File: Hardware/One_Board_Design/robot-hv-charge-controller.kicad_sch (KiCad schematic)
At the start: 14 parts, among them J2 UART_CONN, J3 XT30PW-M, J4 Conn_01x02, J5 XT60PW-M, J6 Conn_01x02, J7 XT60PW-M, J8 Conn_01x03, J9 Conn_01x02

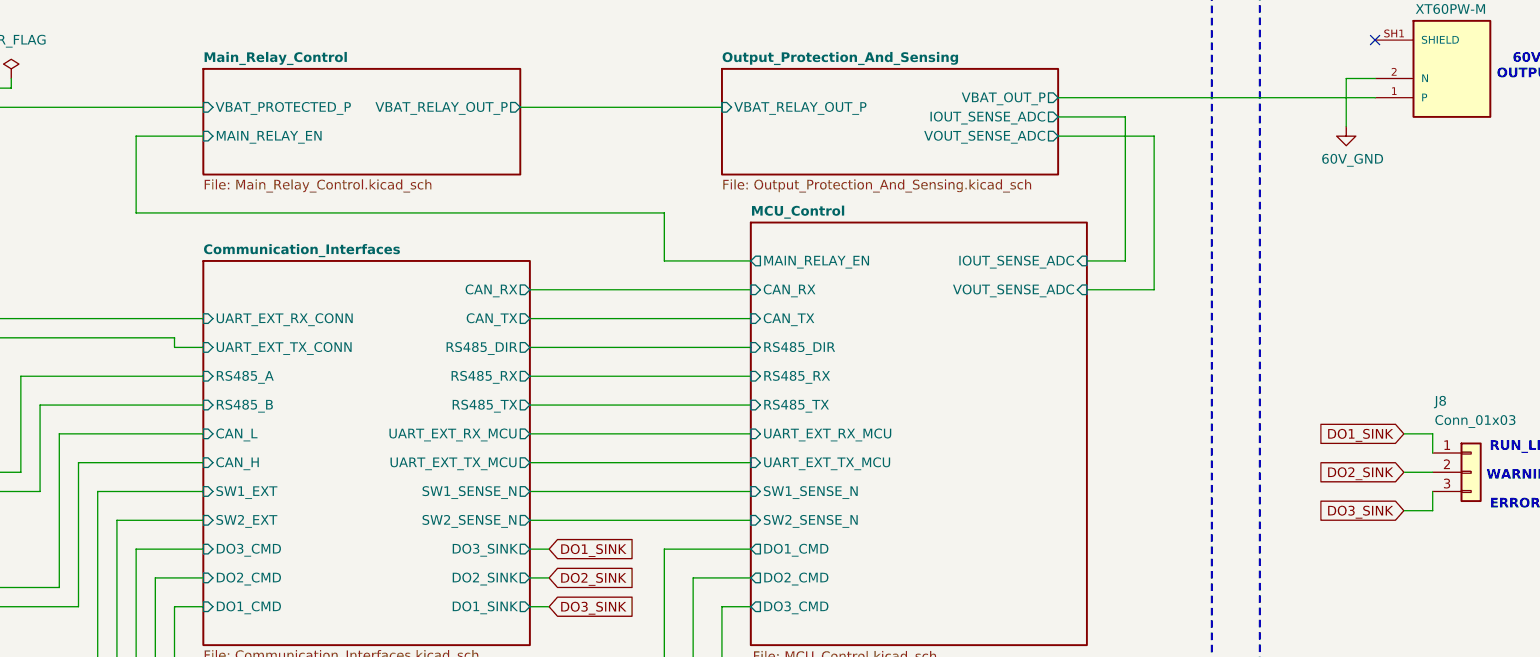
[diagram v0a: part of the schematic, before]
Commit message: refactor(hardware): move KiCad project into One_Board_Design/
Relocate the single-board KiCad project (root schematic, five hierarchical sheets, PCB, project file, and library tables) into Hardware/One_Board_Design/ so the shared symbols, footprints, and 3D models stay in Hardware/libraries/.

Update library tables and 3D model references to use \/../libraries/... so the moved project resolves the shared library location correctly. Replace SparkFun symbol references with the equivalent KiCad standard symbols. Add One_Board_Design README documenting the shared-library layout.

Ultraworked with [Sisyphus](https://github.com/code-yeongyu/oh-my-openagent)

Co-authored-by: Sisyphus <clio-agent@sisyphuslabs.ai>
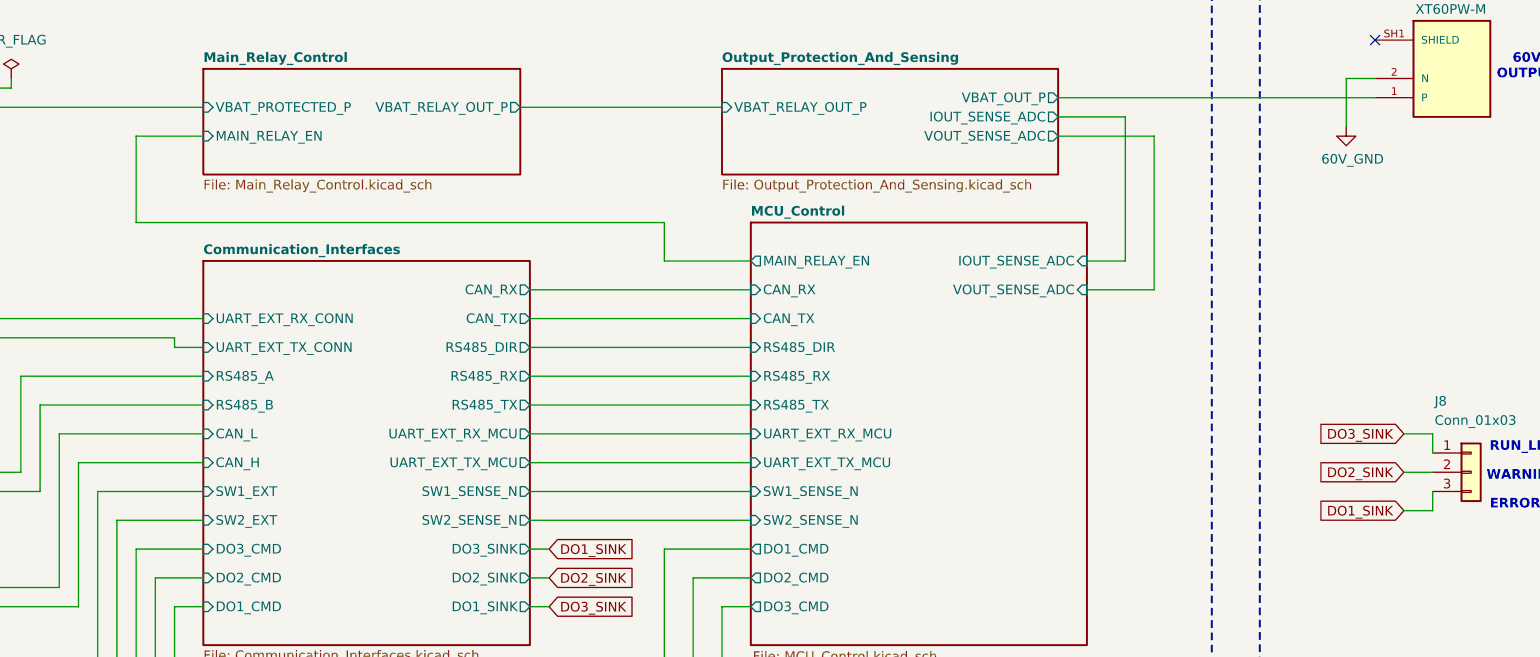
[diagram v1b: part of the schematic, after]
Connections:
- net DO1_SINK: now also J8.3 (Pin_3); no longer J8.1 (Pin_1)
- net DO3_SINK: now also J8.1 (Pin_1); no longer J8.3 (Pin_3)
